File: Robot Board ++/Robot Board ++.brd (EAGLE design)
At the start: 68.6 x 76.2 mm, 124 parts, among them U10 74XX125.RGY, U11 SCHA4B0400, U12 BLUETOOTH-RN41", U13 XBEE-1XBEE-1_LOCK, U5 TPS5331[8/9].DQP, U6 TPS62082.DSG, U7 PCA9557.RGV, U8 MPU-6050

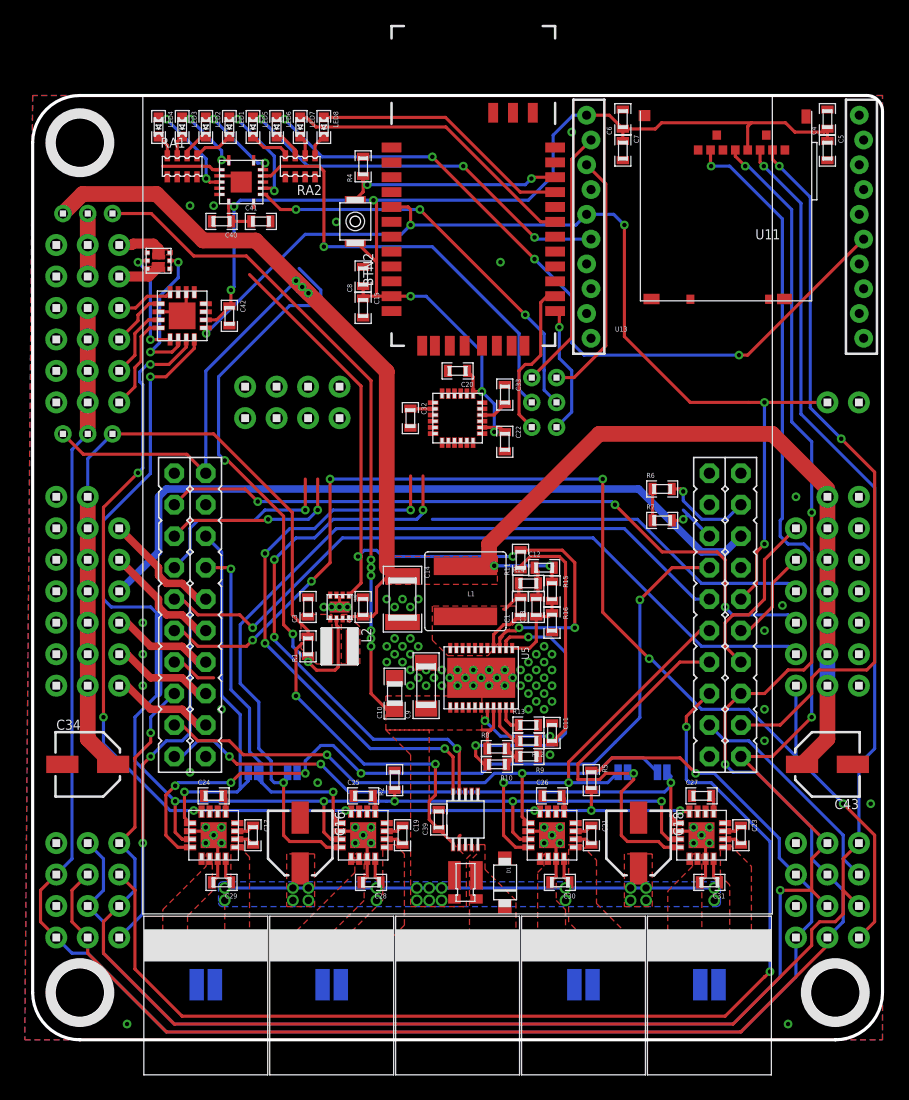
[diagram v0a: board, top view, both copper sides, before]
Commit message: Ripped up all traces. Put as much on the top layer as possible
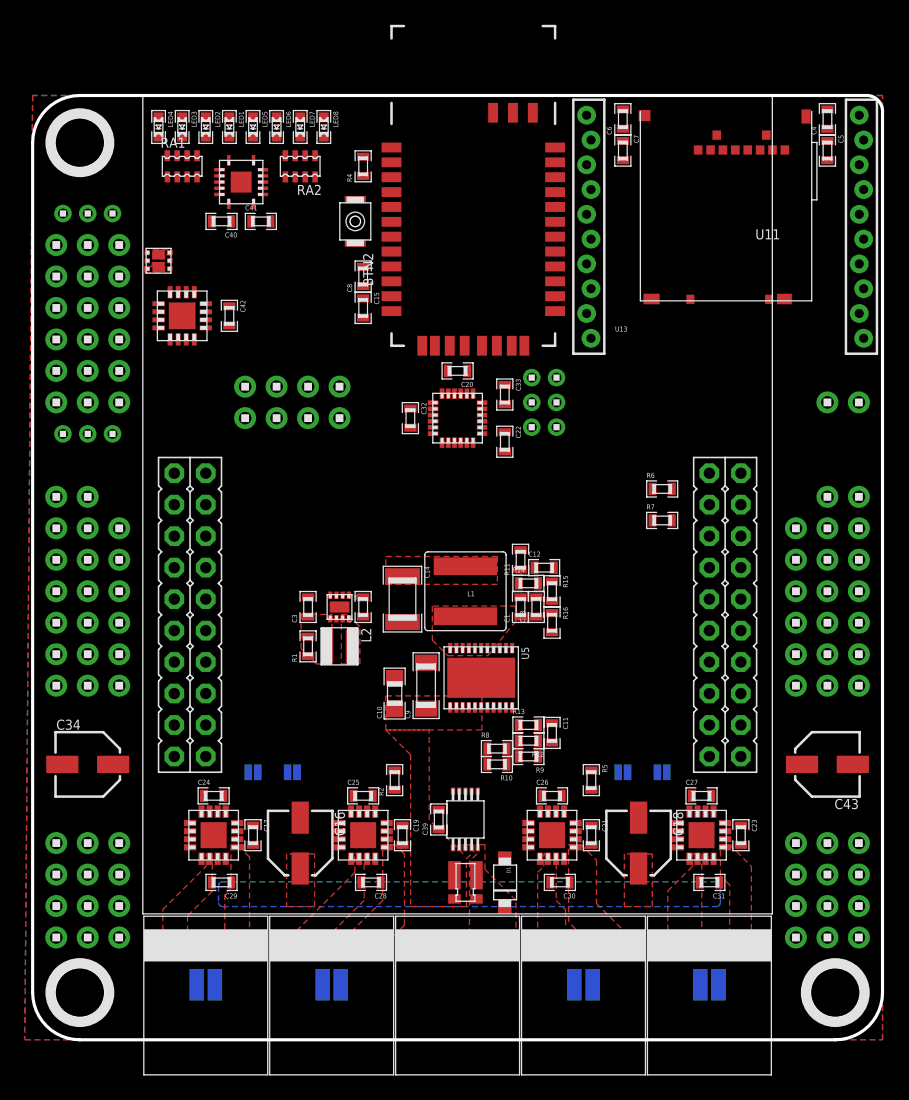
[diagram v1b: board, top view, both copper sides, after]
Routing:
- net 3.3V: track 191.5 -> 0.00 mm, vias 8 -> 0
- net SPI.MOSI: track 159.2 -> 0.00 mm, vias 2 -> 0
- net 5.0V: track 153.6 -> 0.00 mm, vias 5 -> 0
- net SPI.MISO: track 152.5 -> 0.00 mm, vias 3 -> 0
- net SPI.SCLK: track 149.8 -> 0.00 mm, vias 3 -> 0
- net VDDIO: track 148.7 -> 0.00 mm, vias 1 -> 0
- net VBAT: track 114.6 -> 0.00 mm, vias 28 -> 0
- net M.EN: track 103.0 -> 0.00 mm, vias 6 -> 0
- net SVRO5/ENC3.!CS: track 99.3 -> 0.00 mm, vias 6 -> 0
- net ENC0.!CS: track 89.5 -> 0.00 mm, vias 2 -> 0
- net M.MODE: track 89.5 -> 0.00 mm, vias 8 -> 0
- net SVRO4/ENC2.!CS: track 89.3 -> 0.00 mm, vias 3 -> 0
- net !RST: track 85.7 -> 0.00 mm, vias 5 -> 0
- net M1.DIR: track 68.2 -> 0.00 mm, vias 1 -> 0
- net M0.DIR: track 66.2 -> 0.00 mm, vias 5 -> 0
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
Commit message: most power lines routed
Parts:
- removed H25: 1X3, headers(2mm):1X3
- H27: value 1X3 -> 1X2; device headers(2mm):1X3 -> headers(.1in):1X2
- moved L2 3.70 mm to (22.9, 28.6)
- moved R1 3.70 mm to (20.3, 28.6)
- moved C2 3.70 mm to (24.8, 31.8)
- moved C3 3.70 mm to (20.3, 31.8)
- moved U6 3.70 mm to (22.9, 31.8)
- moved U$6 3.18 mm to (20.3, 52.7)
- moved U$7 3.18 mm to (20.3, 50.2)
- moved R13 1.42 mm to (39.4, 26.7)
- moved R14 1.42 mm to (39.4, 38.1)
- moved C1 1.42 mm to (38.7, 36.2)
- moved C13 1.42 mm to (40.0, 36.2)
- moved C39 1.42 mm to (34.0, 18.4)
- moved L1 1.42 mm to (34.3, 37.5)
- moved R10 1.42 mm to (36.8, 23.5)
- moved R11 1.42 mm to (38.7, 40.0)
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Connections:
- net 3.3V: now also H11.1, H11.2, H11.3, H11.4, H13.1, H14.1, H15.1, H16.1; no longer H25.1
- net 5.0V: no longer H25.3, H27.1
- net VBAT: now also H27.2; no longer H27.3
- net VDDIO: no longer H11.1, H11.2, H11.3, H11.4, H13.1, H14.1, H15.1, H16.1, H25.2
- net VIN: now also H27.1; no longer H27.2
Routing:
- net 3.3V: track 0.00 -> 185.9 mm, vias 0 -> 1
- net 5.0V: track 0.00 -> 85.6 mm, vias 0 -> 3
- net VBAT: track 0.00 -> 72.5 mm, vias 0 -> 22
- net GND: track 0.00 -> 37.0 mm, vias 0 -> 78
- net M.EN: track 0.00 -> 14.6 mm
- net AD4: track 0.00 -> 9.72 mm
- net AD5: track 0.00 -> 9.72 mm
- net AD2: track 0.00 -> 8.30 mm
- net AD0: track 0.00 -> 8.30 mm
- net AD1: track 0.00 -> 8.30 mm
- net VIN: track 0.00 -> 5.61 mm
- net M3.DIR: track 0.00 -> 4.62 mm
- net M1.DIR: track 0.00 -> 4.57 mm
- net M2.DIR: track 0.00 -> 4.56 mm
- net M0.DIR: track 0.00 -> 4.50 mm
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
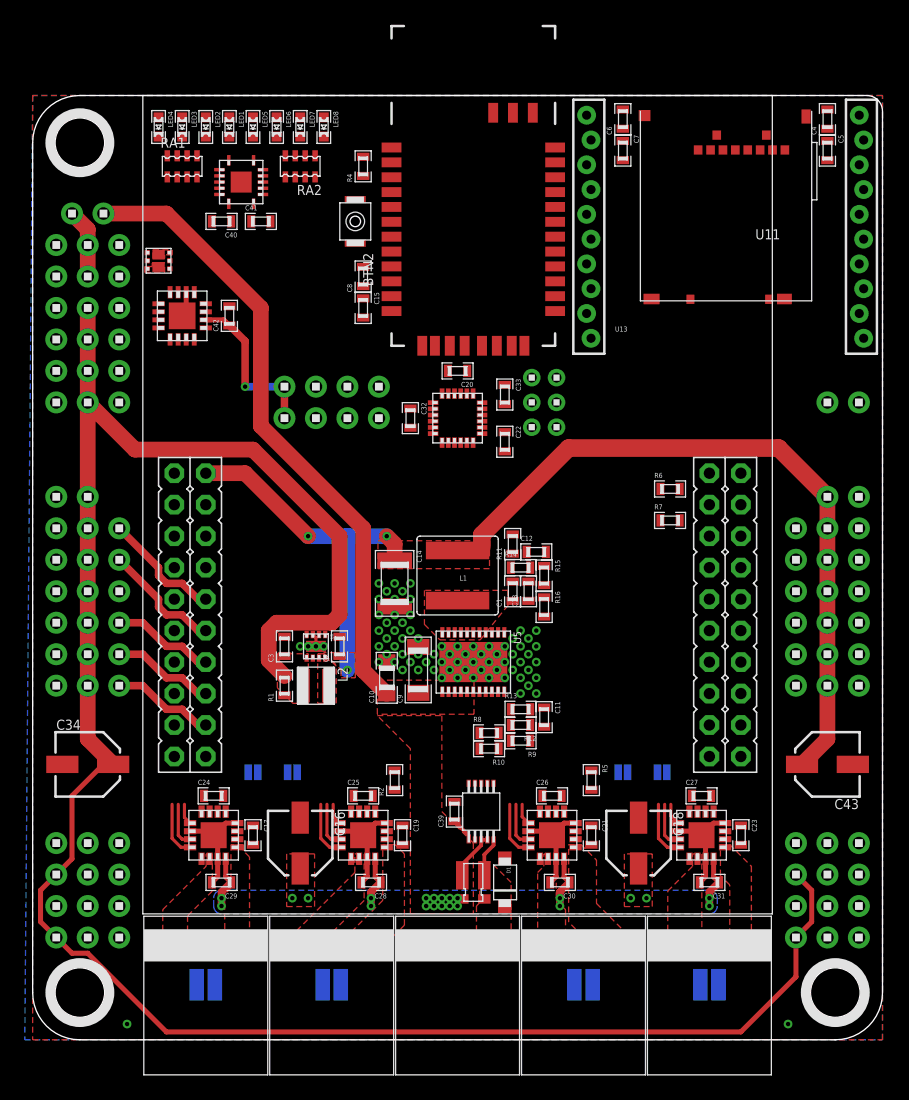
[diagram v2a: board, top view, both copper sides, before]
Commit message: More routing. Most motor control signals completed. Successfully making larger ground plane.
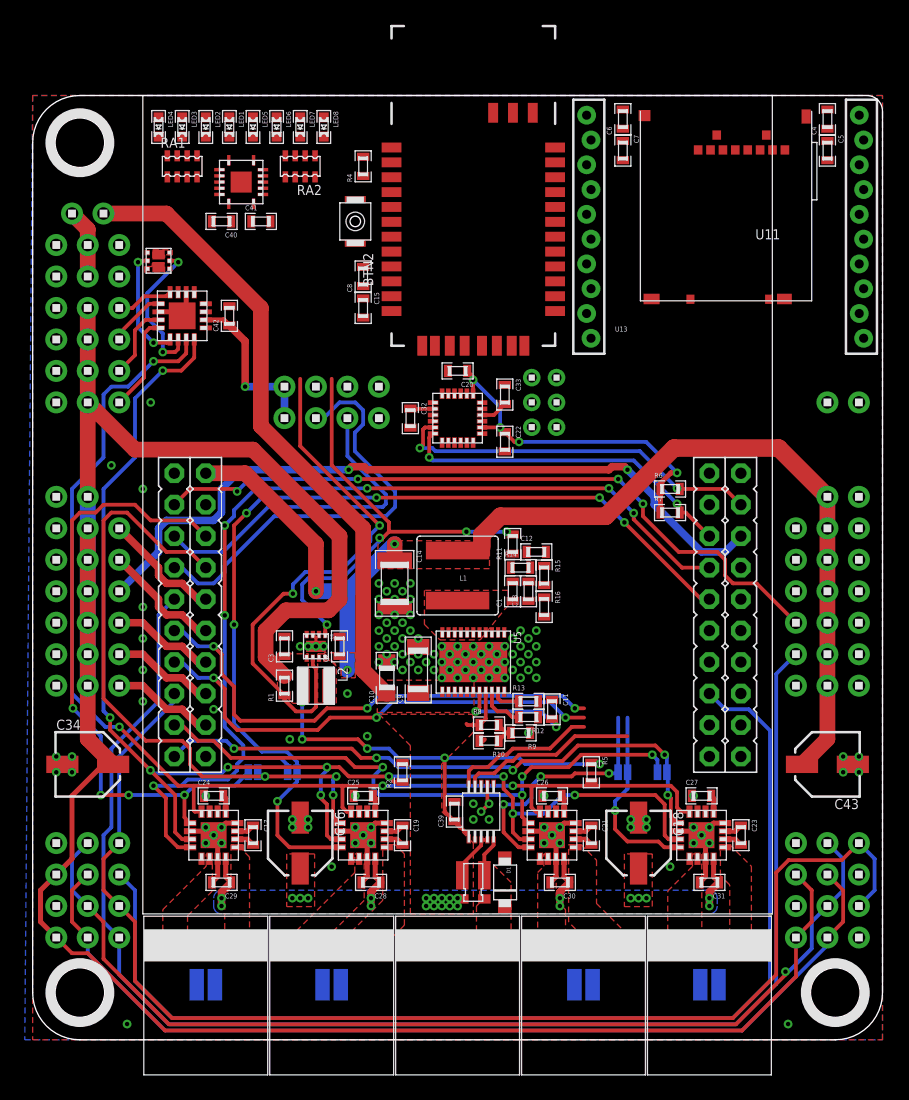
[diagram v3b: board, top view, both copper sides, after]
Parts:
- moved R12 0.90 mm to (40.0, 26.0)
- moved R13 0.90 mm to (40.0, 27.3)
- moved C11 0.90 mm to (41.9, 26.7)
- moved R2 0.90 mm to (29.8, 21.6)
- moved R7 0.64 mm to (51.4, 42.5)
- moved R5 0.64 mm to (45.1, 21.6)
- moved R9 0.64 mm to (39.4, 24.8)
- moved R10 0.63 mm to (36.8, 24.1)
- moved R8 0.63 mm to (36.8, 25.4)
- turned J6 to 180 degrees
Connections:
- removed net VDDIO: R5.1
- net 3.3V: now also R5.1
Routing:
- net SVRO4/ENC2.!CS: track 0.00 -> 116.5 mm
- net SPI.MOSI: track 0.00 -> 103.1 mm
- net M.MODE: track 0.00 -> 97.1 mm, vias 0 -> 4
- net M.EN: track 14.6 -> 108.2 mm, vias 0 -> 10
- net ENC0.!CS: track 0.00 -> 89.2 mm
- net SPI.MISO: track 0.00 -> 83.0 mm, vias 0 -> 1
- net SPI.SCLK: track 0.00 -> 79.3 mm
- net M0.DIR: track 4.50 -> 82.6 mm, vias 0 -> 6
- net 3.3V: track 185.9 -> 261.6 mm, vias 1 -> 10
- net M1.DIR: track 4.57 -> 77.0 mm, vias 0 -> 6
- net AD3: track 0.00 -> 60.5 mm, vias 0 -> 2
- net SVRO3: track 0.00 -> 57.7 mm, vias 0 -> 4
- net M1.SPD: track 1.73 -> 51.7 mm, vias 0 -> 3
- net M0.SPD: track 1.70 -> 50.6 mm, vias 0 -> 4
- net M2.SPD: track 1.73 -> 49.3 mm, vias 0 -> 4
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
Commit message: More routing. Everything below the switching regulators completed!
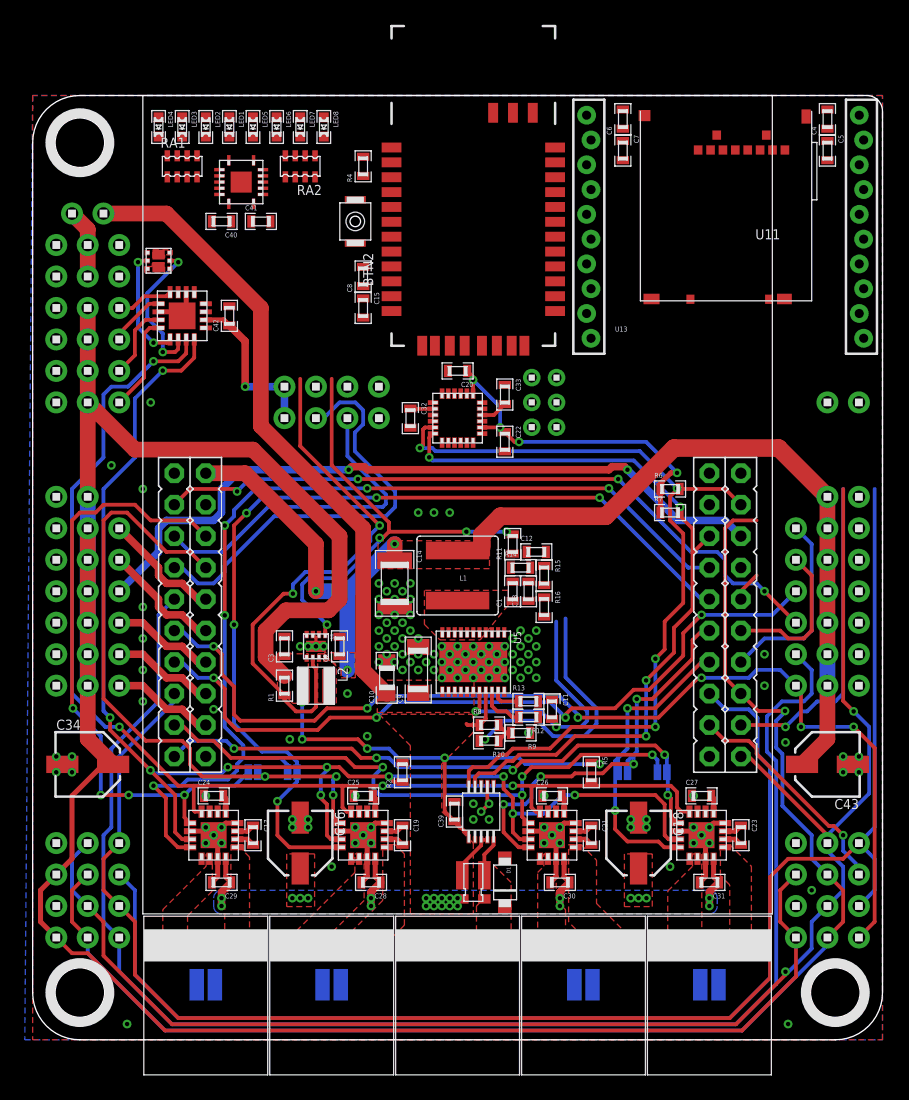
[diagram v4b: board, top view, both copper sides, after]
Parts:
- turned J8 to 0 degrees
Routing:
- net SVRO5/ENC3.!CS: track 39.6 -> 85.2 mm, vias 3 -> 6
- net SPI.MISO: track 83.0 -> 124.0 mm, vias 1 -> 2
- net SPI.SCLK: track 79.3 -> 115.3 mm, vias 0 -> 1
- net SPI.MOSI: track 103.1 -> 131.8 mm
- net I2C.SCL: track 42.1 -> 68.6 mm, vias 2 -> 4
- net SPI.FSS: track 0.00 -> 25.9 mm, vias 0 -> 1
- net SVRO2: track 38.1 -> 60.7 mm, vias 3 -> 4
- net I2C.SDA: track 41.7 -> 62.1 mm, vias 2 -> 4
- net N$8: track 0.49 -> 20.6 mm, vias 0 -> 1
- net ENC1.!CS: track 0.00 -> 18.4 mm, vias 0 -> 1
- net SVRO0: track 0.00 -> 15.5 mm
- net M2.DIR: track 20.1 -> 33.2 mm, vias 3 -> 4
- net SVRO1: track 0.00 -> 12.5 mm
- net N$4: track 9.52 -> 21.3 mm
- net M3.DIR: track 15.1 -> 25.2 mm, vias 1 -> 2
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
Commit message: No airwires left!!! ^_^
Time for a nap...
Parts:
- U10: value 74XX125.RGY -> 74LVTH125.RGY
- turned R11 to 270 degrees
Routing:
- net 3.3V: track 261.6 -> 363.3 mm, vias 10 -> 15
- net !RST: track 2.43 -> 96.9 mm, vias 0 -> 6
- net XBEE.ASSOCIATE: track 0.00 -> 69.7 mm, vias 0 -> 5
- net UART.RXI: track 27.4 -> 71.0 mm, vias 0 -> 3
- net UART.TXO: track 35.2 -> 78.6 mm, vias 0 -> 5
- net SPI.SCLK: track 115.3 -> 152.0 mm, vias 1 -> 3
- net SPI.MISO: track 124.0 -> 160.3 mm
- net XBEE.RSSI: track 0.00 -> 35.4 mm, vias 0 -> 3
- net 5V.PG: track 38.2 -> 72.9 mm, vias 4 -> 8
- net SPI.MOSI: track 131.8 -> 166.4 mm, vias 0 -> 3
- net SPI.FSS: track 25.9 -> 59.6 mm, vias 1 -> 2
- net I2C.SDA: track 62.1 -> 95.4 mm, vias 4 -> 7
- net I2C.SCL: track 68.6 -> 101.2 mm, vias 4 -> 7
- net BT.STATUS: track 0.00 -> 27.2 mm
- net BT.CONNECT: track 0.00 -> 26.2 mm
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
